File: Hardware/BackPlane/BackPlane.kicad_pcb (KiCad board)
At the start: 2 copper layers, 117 x 97 mm, 19 parts, among them J101 CAN, J102 i²c, J103 Power Harness, J104 GPIO, U101 COMPUTER, U102 CARD 0, U103 CARD 1, U104 CARD 2, U105 CARD 3

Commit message: Bump to fix broken reference
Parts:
- renumbered G*** to LOGO1
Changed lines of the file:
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@@
 		(layer "F.Cu")
 		(at 90.5 72 90)
-		(property "Reference" "G***"
+		(property "Reference" "LOGO1"
 			(at 0 0 90)
-			(layer "F.SilkS")
+			(layer "F.Fab")
 			(effects
 				(font

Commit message: Bump backplane
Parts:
- removed J101: CAN, Connector_JST:JST_EH_B3B-EH-A_1x03_P2.50mm_Vertical
- removed J103: Power Harness, Connector_JST:JST_EH_B5B-EH-A_1x05_P2.50mm_Vertical
- added J1: CAN, Connector_Wire:SolderWire-0.5sqmm_1x02_P4.6mm_D0.9mm_OD2.1mm_Relief, F.Cu at (60.0, -10.5)
- added J2: Power Harness, Connector_Wire:SolderWire-0.25sqmm_1x03_P4.5mm_D0.65mm_OD2mm_Relief, F.Cu at (-71.5, 2.88)
- added J3: CAN, Connector_Wire:SolderWire-0.5sqmm_1x02_P4.6mm_D0.9mm_OD2.1mm_Relief, F.Cu at (-60.0, -15.0)
- moved H101 172.0 mm to (-55.0, -45.0)
- moved H102 172.0 mm to (-55.0, 45.0)
- moved H103 172.0 mm to (55.0, -45.0)
- moved H104 172.0 mm to (55.0, 45.0)
- moved J102 172.0 mm to (52.5, 8.00)
- moved J104 172.0 mm to (52.5, -3.50)
- moved LOGO1 172.0 mm to (-49.5, -28.0)
- moved LOGO2 172.0 mm to (-11.0, 6.50)
- moved REF** 172.0 mm to (-47.5, -14.5)
- moved REF** 172.0 mm to (-47.5, -38.5)
- moved TP101 172.0 mm to (50.0, 23.9)
- moved TP102 172.0 mm to (30.5, 38.5)
- moved U101 172.0 mm to (-40.0, 0.04)
- moved U102 172.0 mm to (-20.0, 0.00)
- moved U103 172.0 mm to (0.00, 0.00)
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- renumbered G*** to LOGO2
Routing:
- net /CANH: track 102.2 -> 140.1 mm
- net /CANL: track 107.3 -> 143.5 mm, vias 0 -> 1
- net +12V: track 210.7 -> 203.9 mm
- net +5V: track 135.2 -> 141.0 mm
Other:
- board size 117 x 97 mm -> 150 x 97 mm

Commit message: Remove bad ref**
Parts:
- renumbered REF** to LOGO3, REF** to LOGO5
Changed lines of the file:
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@@
 		(descr "KiCad Logo")
 		(tags "Logo KiCad")
-		(property "Reference" "REF**"
+		(property "Reference" "LOGO5"
 			(at 0 -5.08 90)
 			(layer "F.SilkS")
@@
 			(at 0 0 90)
 			(layer "F.Fab")
+			(hide yes)
 			(effects
 				(font
@@
 		(tags "connector wire 0.5sqmm strain-relief")
 		(property "Reference" "J1"
-			(at 2.3 -2.25 270)
+			(at 2.3 -2.25 -90)
 			(layer "F.SilkS")
 			(effects
@@
 		)
 		(property "Value" "CAN"
-			(at 2.3 15.1 270)
+			(at 2.3 15.1 -90)
 			(layer "F.Fab")
 			(effects
@@
 		)
 		(fp_text user "${REFERENCE}"
-			(at 2.3 6.3 360)
+			(at 2.3 6.3 0)
 			(layer "F.Fab")
 			(effects
@@
 		(descr "Open Source Hardware Symbol")
 		(tags "Logo Symbol OSHW")
-		(property "Reference" "REF**"
+		(property "Reference" "LOGO3"
 			(at 0 0 90)
 			(layer "F.SilkS")

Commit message: Prep for backplane proto
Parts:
- removed H101, H102, H103, H104: MountingHole, MountingHole:MountingHole_3.5mm
- added H1: MountHole, MountingHole:MountingHole_3.5mm_Pad, F.Cu at (55.0, 45.0)
- added H2: MountHole, MountingHole:MountingHole_3.5mm_Pad, F.Cu at (55.0, -45.0)
- added H3: MountHole, MountingHole:MountingHole_3.5mm_Pad, F.Cu at (-55.0, -45.0)
- added H4: MountHole, MountingHole:MountingHole_3.5mm_Pad, F.Cu at (-55.0, 45.0)
- J102: footprint Connector_JST:JST_EH_B3B-EH-A_1x03_P2.50mm_Vertical -> Connector_Wire:SolderWire-0.25sqmm_1x03_P4.5mm_D0.65mm_OD2mm_Relief; moved to F.Cu
- J104: footprint Connector_JST:JST_EH_B5B-EH-A_1x05_P2.50mm_Vertical -> Connector_Wire:SolderWire-0.5sqmm_1x05_P4.6mm_D0.9mm_OD2.1mm_Relief; moved to F.Cu
- moved J104 29.5 mm to (60.0, 25.0)
- moved J102 9.30 mm to (60.0, 2.50)
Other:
- outline, holes or cut-outs redrawn
- board text added: "${FULL_REVISION}"
- board text added: "I2C_CLK"
- board text added: "I2C_SDA"
- board text added: "JLCJLCJLCJLC"

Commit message: So near to a backplane prototype now
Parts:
- added F1: Fuse, Fuse:Fuseholder_Littelfuse_100_series_5x20mm, B.Cu at (-72.0, -5.00)
- added REF**: EBM15DSEH, KenwoodFox:EBM15DSEH_Blank, F.Cu at (-60.0, 0.00)
- added REF**: EBM15DSEH, KenwoodFox:EBM15DSEH_Blank, F.Cu at (40.0, 0.00)
- U102: value CARD 0 -> CARD 1
- U103: value CARD 1 -> CARD 2
- U104: value CARD 2 -> CARD 3
- U105: value CARD 3 -> CARD 4
- moved TP101 23.2 mm to (73.0, 27.0)
- moved H1 20.0 mm to (75.0, 45.0)
- moved H2 20.0 mm to (75.0, -45.0)
- moved H3 20.0 mm to (-75.0, -45.0)
- moved H4 20.0 mm to (-75.0, 45.0)
- moved J1 20.0 mm to (80.0, -10.5)
- moved J102 20.0 mm to (80.0, 2.50)
- moved J104 20.0 mm to (80.0, 25.0)
- moved J2 20.0 mm to (-91.5, 2.88)
- moved J3 20.0 mm to (-80.0, -15.0)
- moved U105 20.0 mm to (60.0, 0.00)
- moved LOGO1 0.50 mm to (-50.0, -28.0)
- moved LOGO3 0.50 mm to (-48.0, -38.5)
- moved LOGO5 0.50 mm to (-48.0, -14.5)
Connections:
- J2 pad 3: +12V -> Net-(J2-Pin_3)
- U101 pad 10: /CARD_SEL_3 -> /CARD_SEL_4
- U101 pad 3: /CARD_EN_0 -> /CARD_EN_1
- U101 pad 4: /CARD_SEL_0 -> /CARD_SEL_1
- U101 pad 5: /CARD_EN_1 -> /CARD_EN_2
- U101 pad 6: /CARD_SEL_1 -> /CARD_SEL_2
- U101 pad 7: /CARD_EN_2 -> /CARD_EN_3
- U101 pad 8: /CARD_SEL_2 -> /CARD_SEL_3
- U101 pad 9: /CARD_EN_3 -> /CARD_EN_4
- U102 pad 3: /CARD_EN_0 -> /CARD_EN_1
- U102 pad 4: /CARD_SEL_0 -> /CARD_SEL_1
- U103 pad 3: /CARD_EN_1 -> /CARD_EN_2
- U103 pad 4: /CARD_SEL_1 -> /CARD_SEL_2
- U104 pad 3: /CARD_EN_2 -> /CARD_EN_3
- U104 pad 4: /CARD_SEL_2 -> /CARD_SEL_3
- U105 pad 3: /CARD_EN_3 -> /CARD_EN_4
- U105 pad 4: /CARD_SEL_3 -> /CARD_SEL_4
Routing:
- net /CARD_EN_4: track 0.00 -> 106.6 mm
- net /CARD_SEL_4: track 0.00 -> 104.9 mm
- net /GPIO3: track 107.5 -> 154.8 mm, vias 0 -> 1
- net /GPIO2: track 103.0 -> 146.1 mm, vias 0 -> 1
- net /CANL: track 143.5 -> 183.5 mm
- net /CANH: track 140.1 -> 180.1 mm
- net +5V: track 141.0 -> 181.0 mm
- net /GPIO1: track 103.0 -> 141.9 mm, vias 0 -> 1
- net +12V: track 203.9 -> 237.3 mm
- net /I2C_CLK: track 103.6 -> 137.0 mm, vias 0 -> 1
- net /I2C_SDA: track 102.3 -> 131.7 mm
- net /CARD_EN_1: track 43.3 -> 21.6 mm
- net /CARD_SEL_2: track 64.7 -> 43.1 mm
- net /CARD_EN_3: track 86.6 -> 64.9 mm
- net /CARD_EN_2: track 64.9 -> 43.3 mm
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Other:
- board size 150 x 97 mm -> 190 x 97 mm
- board text added: "BLANK CARD"
- board text removed: "+12v"
- board text removed: "SCL"
- board text removed: "SDA"

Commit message: Remove broken refs
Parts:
- renumbered REF** to BLANK1, REF** to BLANK2
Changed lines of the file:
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@@
 		(layer "F.Cu")
 		(at -60 0 90)
-		(property "Reference" "REF**"
+		(property "Reference" "BLANK1"
 			(at -40.25 -5 90)
 			(unlocked yes)
@@
 		(layer "F.Cu")
 		(at 40 0 90)
-		(property "Reference" "REF**"
+		(property "Reference" "BLANK2"
 			(at -40.25 -5 90)
 			(unlocked yes)
@@
 		(tags "connector wire 0.25sqmm strain-relief")
 		(property "Reference" "J102"
-			(at 4.5 -2.2 270)
+			(at 4.5 -2.2 -90)
 			(layer "F.SilkS")
 			(hide yes)
@@
 		(tags "connector wire 0.5sqmm strain-relief")
 		(property "Reference" "J1"
-			(at 2.3 -2.25 270)
+			(at 2.3 -2.25 -90)
 			(layer "F.SilkS")
 			(hide yes)
@@
 		(tags "connector wire 0.5sqmm strain-relief")
 		(property "Reference" "J104"
-			(at 9.2 -2.25 270)
+			(at 9.2 -2.25 -90)
 			(layer "F.SilkS")
 			(hide yes)

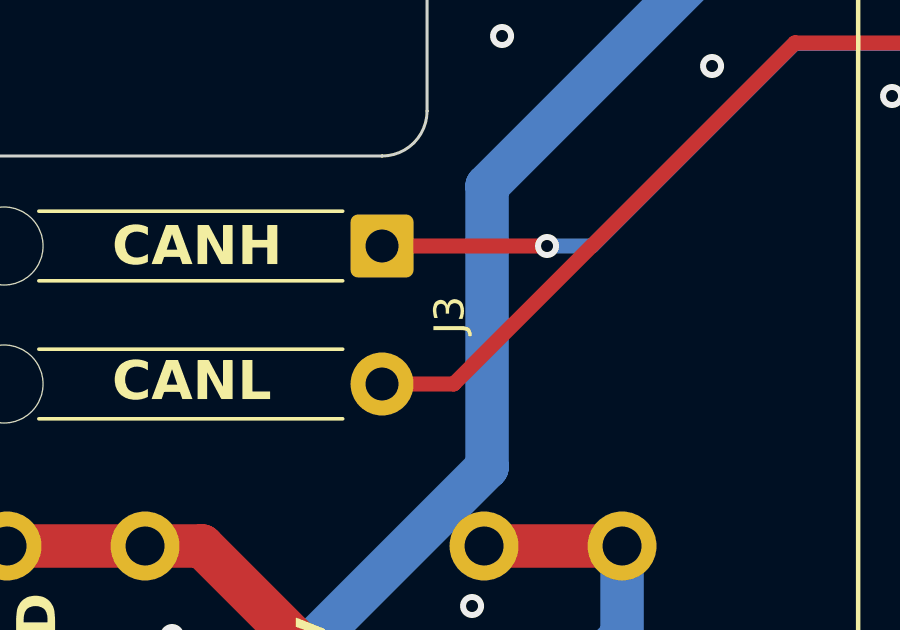
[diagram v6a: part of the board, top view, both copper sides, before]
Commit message: Plot footprint values for JLC export
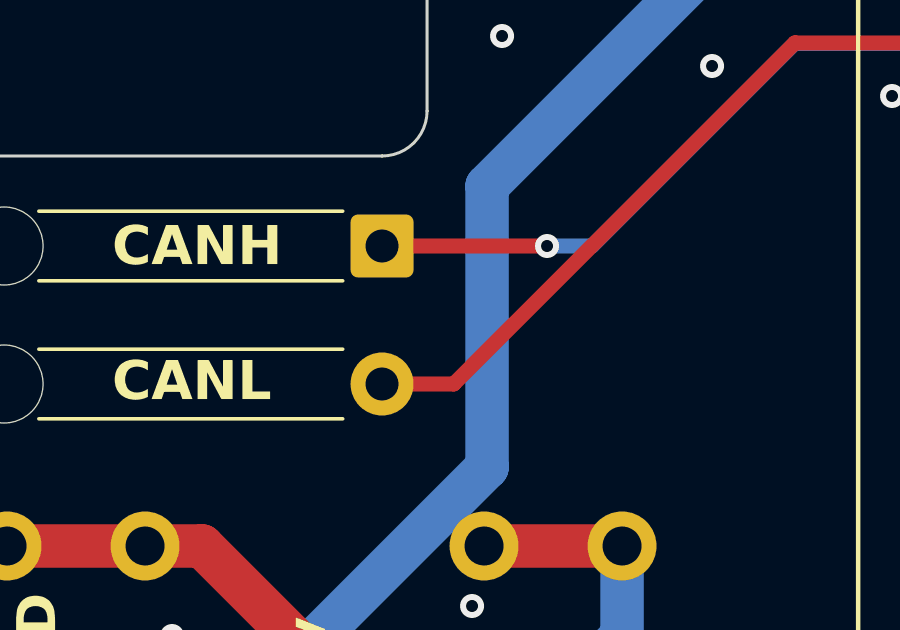
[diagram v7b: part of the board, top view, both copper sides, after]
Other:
- board text added: "FUSE"
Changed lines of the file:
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@@
 			(at 2.3 -2.25 90)
 			(layer "F.SilkS")
+			(hide yes)
 			(effects
 				(font
@@
 			(unlocked yes)
 			(layer "B.SilkS")
+			(hide yes)
 			(effects
 				(font
@@
 		)
 	)
+	(gr_text "FUSE"
+		(at -82 -5 0)
+		(layer "B.SilkS")
+		(effects
+			(font
+				(size 1.5 1.5)
+				(thickness 0.3)
+				(bold yes)
+			)
+			(justify mirror)
+		)
+	)
